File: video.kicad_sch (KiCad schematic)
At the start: 75 parts, among them IC11 MC14053, IC14 74LS86AN, IC21 74LS74, IC22 74LS00N, IC23 74ALS74N, IC27 74LS20N, IC28 74LS393N, IC29 74LS393N, IC30 74LS32N, IC32 74LS390, IC44 MC3346, U1 LINE_PULSE_DIAGRAM

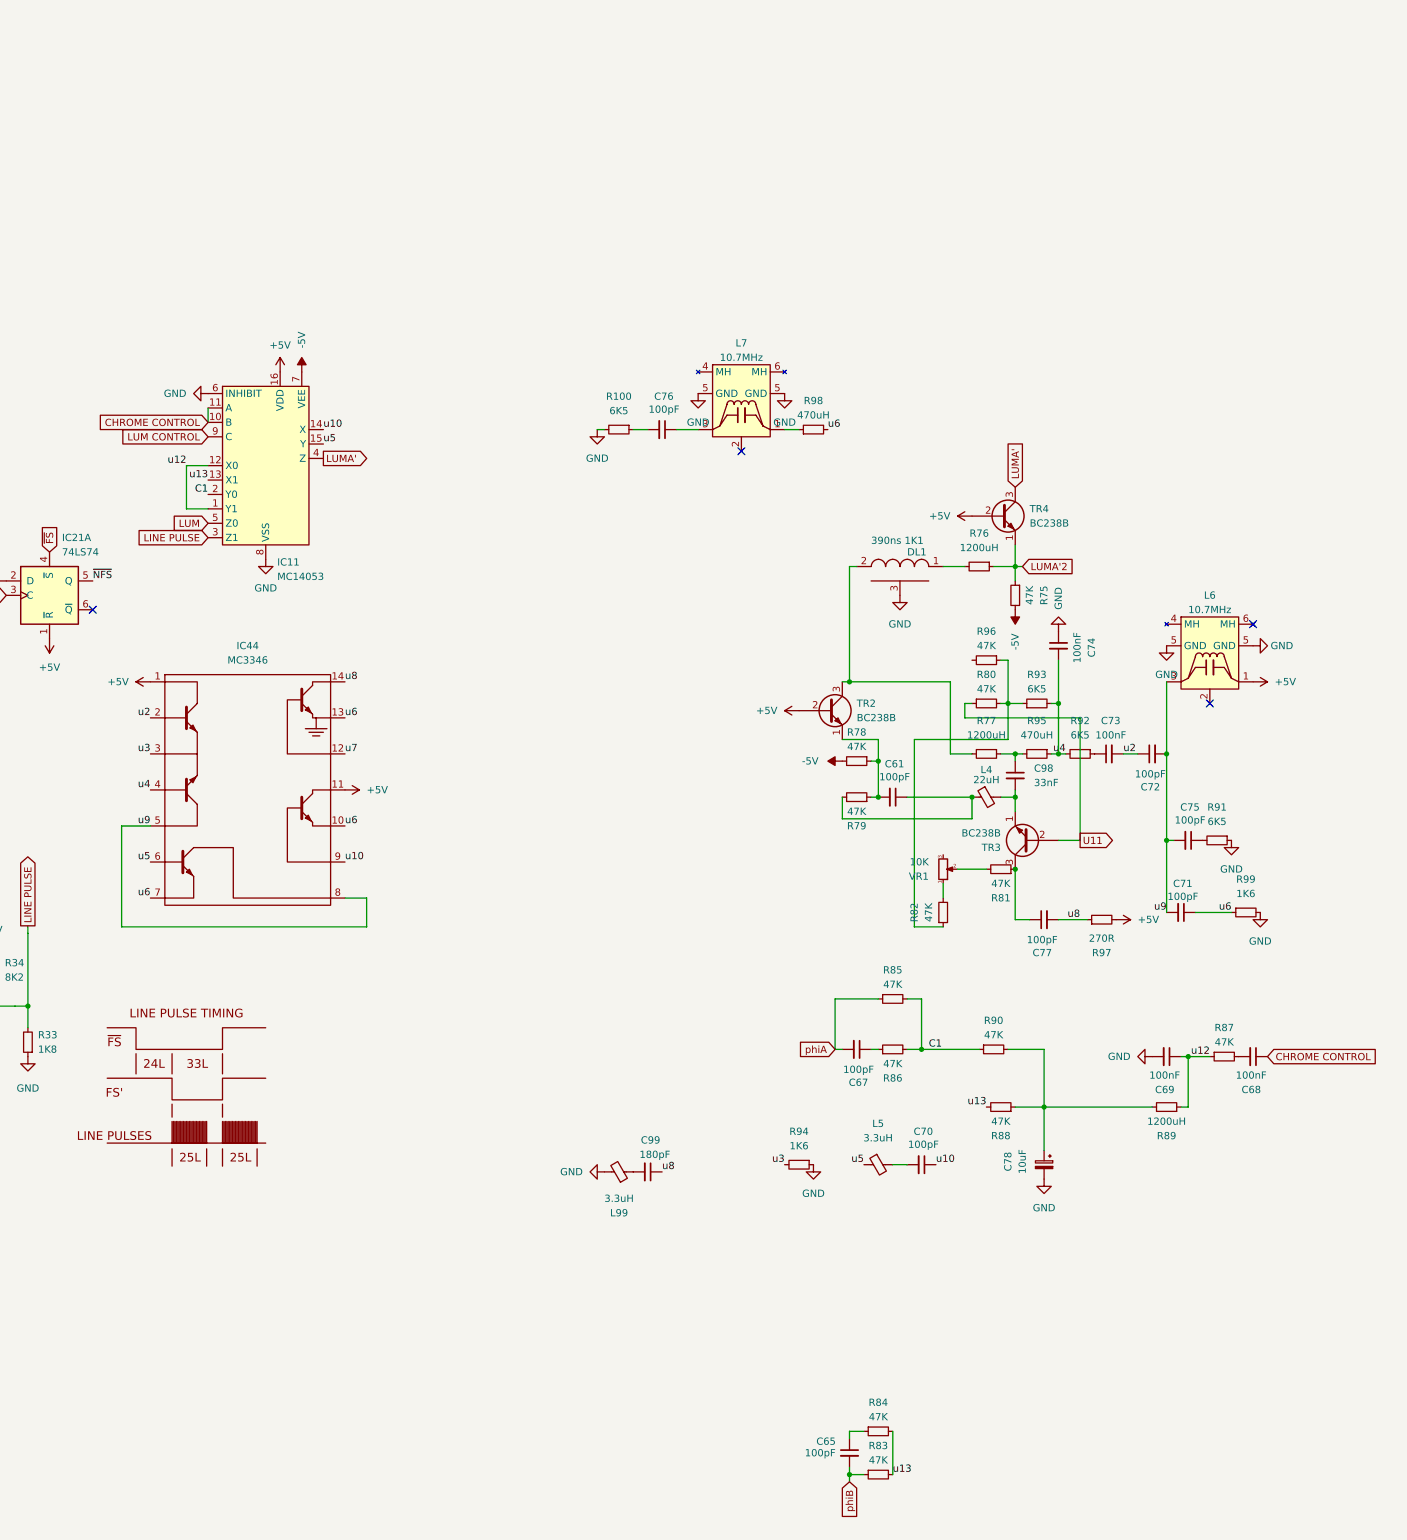
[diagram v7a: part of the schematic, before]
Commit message: resolve missing connections
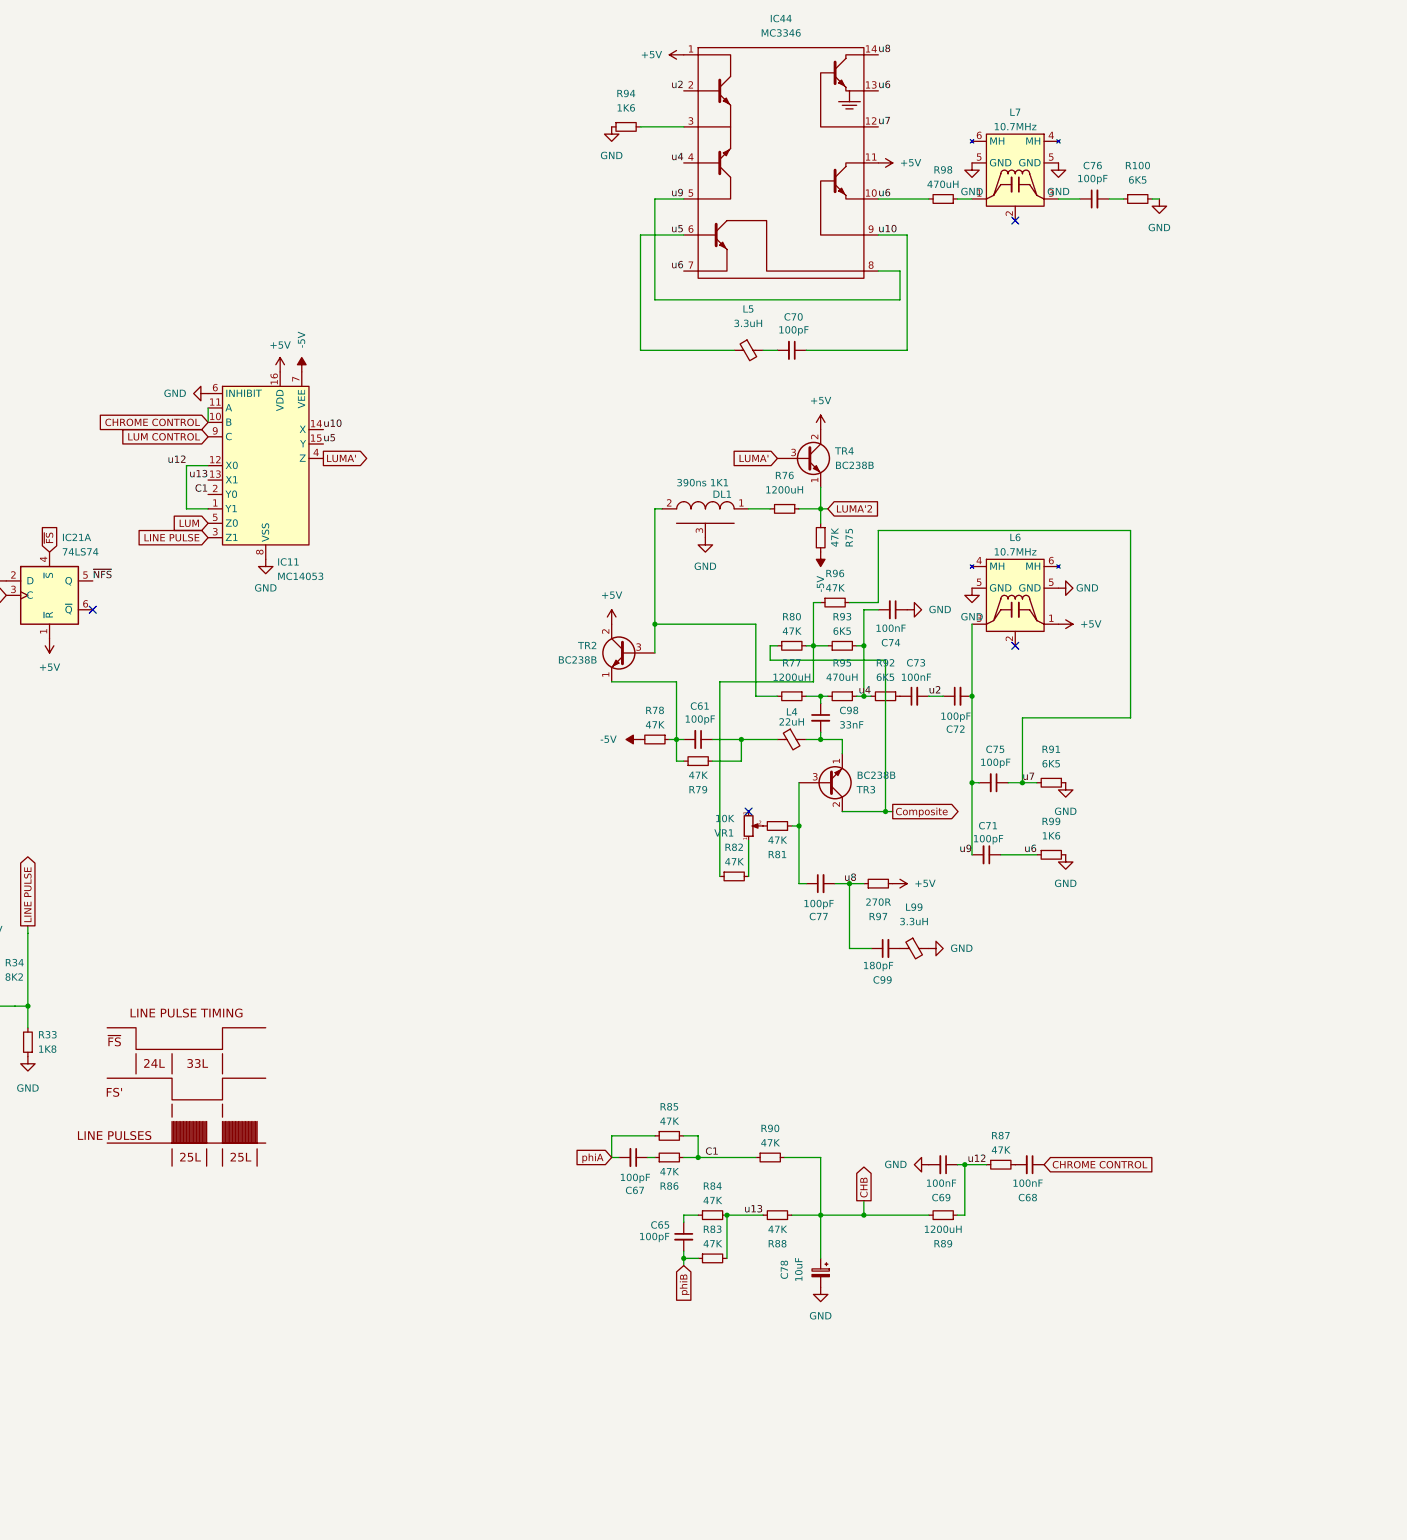
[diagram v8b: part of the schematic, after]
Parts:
- removed TR2, TR3, TR4: BC238B, Package_TO_SOT_THT:TO-92, symbol Device:Q_NPN_EBC
- added TR2, TR3, TR4: BC238B, Package_TO_SOT_THT:TO-92, symbol Device:Q_NPN_ECB
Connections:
- net +5V: now also TR2.2 (C), TR4.2 (C)
- net LUMA': now also TR4.3 (B)
- net LUMA'2: now also TR4.1 (E)
- net u7: now also C75.1, R91.2, R96.2
- net at DL1.2, R77.2: now also TR2.3 (B)
- net at C77.1, R81.1: now also TR3.3 (B)
- net at C98.2, L4.2: now also TR3.1 (E)
- net at C61.2, R78.1, R79.1: now also TR2.1 (E)
- net CHB: now reaches C78.1, R88.1, R89.2, R90.2
- net U11 renamed Composite
- net Composite: now also TR3.2 (C)
- net u3: no longer names the net of IC44.3, R94.2
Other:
- moved on the sheet: C61, C65, C67, C68, C69, C70, C71, C72, C73, C74, C75, C76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
